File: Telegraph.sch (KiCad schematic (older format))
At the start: 16 parts

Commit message: Bump to v2 and add board layout
This design is intended for using a Raspberry Pi W and adds a header to
connect the Raspberry pi directly to the board. This also adds a PCB
speaker along with a transistor to amplify it, and a switching power
supply (prefab module). The transistor for the magnets is replaced by a
MOSFET (which has better specs and mostly a cuter package than the
TIP12x that was on there).
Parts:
- removed SHIELD?: ARDUINO_UNO, symbol ARDUINO_UNO
- removed U?: POLOLU_DRV8825, symbol POLOLU_DRV8825
- added A1: Pololu_Breakout_DRV8825, Modules:Pololu_Breakout-16_15.2x20.3mm, symbol Pololu_Breakout_DRV8825
- added C2, C3: 10uF, Capacitors_THT:CP_Radial_D5.0mm_P2.00mm, symbol CP
- added J1: Raspberry_Pi_2_3, Footprints:Raspberry_Pi_Zero, symbol Raspberry_Pi_2_3
- added P1: SPK, Pin_Headers:Pin_Header_Angled_1x02_Pitch2.54mm, symbol CONN_01X02
- added P5: FTDI-DEVICE, Pin_Headers:Pin_Header_Angled_1x06_Pitch2.54mm, symbol FTDI-DEVICE
- added Q1: STU60N3LH5, TO_SOT_Packages_THT:TO-251AA, symbol STU60N3LH5
- added R1: 1K, Resistors_THT:R_Axial_DIN0207_L6.3mm_D2.5mm_P10.16mm_Horizontal, symbol R
- added R2: 47R, Resistors_THT:R_Axial_DIN0207_L6.3mm_D2.5mm_P10.16mm_Horizontal, symbol R
- added REG1: REGULATOR_MODULE, Footprints:HCJ-IPM-V2, symbol REGULATOR_MODULE
- added RV1: 1K, Potentiometers:Potentiometer_Trimmer_ACP_CA9v_Horizontal_Px10.0mm_Py5.0mm, symbol POT
- added SW1: SW_Push, Buttons_Switches_THT:SW_Tactile_SPST_Angled_PTS645Vx58-2LFS, symbol SW_Push
- C1: renamed from C?; footprint (none) -> Capacitors_THT:CP_Radial_D8.0mm_P3.50mm
- CON1: renamed from CON?; footprint (none) -> Connectors:BARREL_JACK
- D1: renamed from D?; footprint (none) -> Diodes_THT:D_DO-41_SOD81_P10.16mm_Horizontal
- JP1: renamed from JP?; value Jumper_NO_Small -> A4988; footprint (none) -> Pin_Headers:Pin_Header_Straight_1x02_Pitch2.54mm
- JP2: renamed from JP?; value Jumper_NO_Small -> M0; footprint (none) -> Pin_Headers:Pin_Header_Straight_1x02_Pitch2.54mm
- JP3: renamed from JP?; value Jumper_NO_Small -> M1; footprint (none) -> Pin_Headers:Pin_Header_Straight_1x02_Pitch2.54mm
- JP4: renamed from JP?; value Jumper_NO_Small -> M2; footprint (none) -> Pin_Headers:Pin_Header_Straight_1x02_Pitch2.54mm
- P2, P4: renamed from P?; footprint (none) -> Pin_Headers:Pin_Header_Angled_1x02_Pitch2.54mm
- P3: renamed from P?; footprint (none) -> Pin_Headers:Pin_Header_Angled_1x04_Pitch2.54mm
- Q2: renamed from Q?; value TIP120 -> STU60N3LH5; footprint TO-220 -> TO_SOT_Packages_THT:TO-251AA; symbol TIP120 -> STU60N3LH5
- R3, R4: renamed from R?; footprint (none) -> Resistors_Universal:Resistor_SMD+THTuniversal_0805to1206_RM10_HandSoldering
- SP1: renamed from SP?; footprint (none) -> Buzzers_Beepers:Buzzer_15x7.5RM7.6
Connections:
- net +12V: now also A1.8 (VMOT), C2.1, REG1.2 (IN+)
- net +5V: now also JP2.1, JP3.1, JP4.1, A1.13 (~RST), A1.14 (~SLP), C3.1, J1.2 (5V), J1.4 (5V), R2.1, REG1.4 (OUT+); no longer JP2.2, JP3.2, JP4.2
- net DIR: now also A1.16 (DIR), J1.31 (GPIO6)
- net EN: now also A1.9 (~EN), J1.37 (GPIO26)
- net GND: now also A1.1 (GND), A1.7 (GND), C2.2, C3.2, J1.14 (GND), J1.20 (GND), J1.25 (GND), J1.30 (GND), J1.34 (GND), J1.39 (GND), J1.6 (GND), J1.9 (GND), P5.1 (GND), Q1.3 (S), REG1.1 (IN-), REG1.3 (OUT-), SW1.1; no longer SP1.2
- net KEY: now also J1.11 (GPIO17_(GEN0))
- net MAGNET: now also J1.36 (GPIO16)
- net SPK: now also J1.12 (GPIO18_(GEN1)), R1.2; no longer SP1.1
- net STEP: now also A1.15 (STEP), J1.33 (GPIO13)
- net at JP1.2: now also A1.2 (~FLT)
- net at P3.1 (P1): now also A1.6 (B2)
- net at P3.2 (P2): now also A1.5 (B1)
- net at P3.3 (P3): now also A1.4 (A1)
- net at P3.4 (P4): now also A1.3 (A2)
- new net: A1.11 (M1), JP3.2
- new net: A1.12 (M2), JP4.2
- new net: A1.10 (M0), JP2.2
- new net: P1.2 (P2), RV1.1, SP1.1
- new net: P1.1 (P1), Q1.2 (D), SP1.2
- new net: Q1.1 (G), R1.1
- new net: R2.2, RV1.2
- new net PWR: J1.5 ((SCL1)_GPIO3), SW1.2
- new net RX: J1.10 ((RXD0)_GPIO15), P5.4 (RX)
- new net TX: J1.8 ((TXD0)_GPIO14), P5.5 (TX)
- no-connect marks 1 -> 26
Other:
- moved on the sheet: C1, CON1, D1, P2, P3, P4, R3, R4, SP1

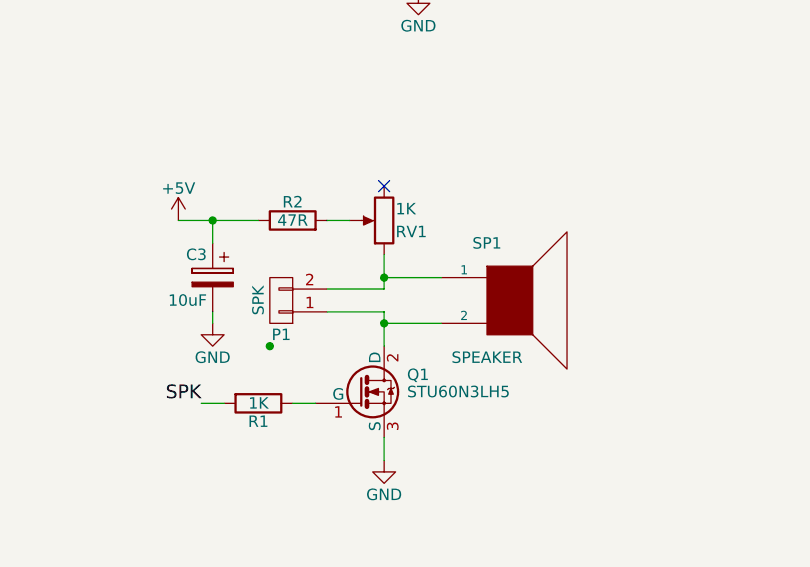
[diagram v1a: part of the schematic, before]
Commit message: Improve values for speaker
The previous resistor values were more conservative, based on another
speaker.  Testing with the actual speaker, whose type number was also
addd to the schematic, suggests smaller resistor values will work
better.
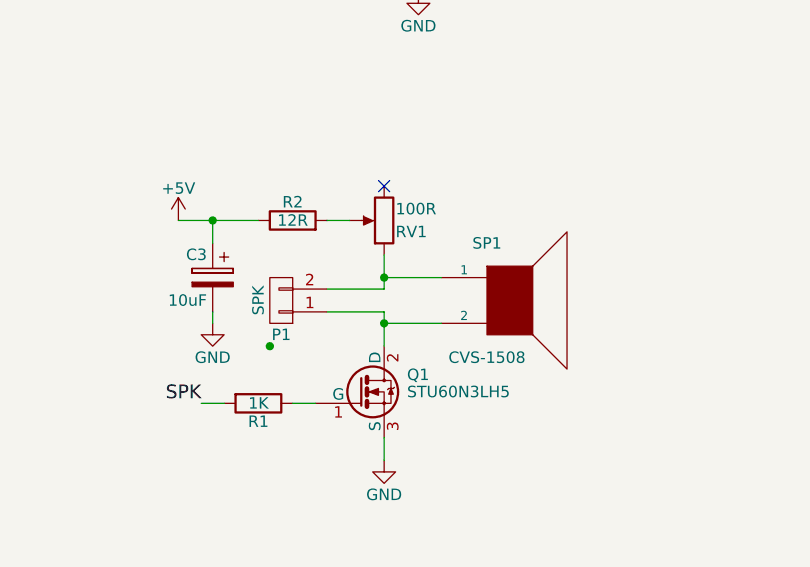
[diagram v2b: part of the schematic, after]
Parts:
- R2: value 47R -> 12R
- RV1: value 1K -> 100R
- SP1: value SPEAKER -> CVS-1508
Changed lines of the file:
@@
 P 7550 4100
 F 0 "SP1" H 7450 4350 50  0000 C CNN
-F 1 "SPEAKER" H 7450 3850 50  0000 C CNN
+F 1 "CVS-1508" H 7450 3850 50  0000 C CNN
 F 2 "Buzzers_Beepers:Buzzer_15x7.5RM7.6" H 7550 4100 50  0001 C CNN
 F 3 "" H 7550 4100 50  0000 C CNN
@@
 P 6600 3750
 F 0 "R2" V 6680 3750 50  0000 C CNN
-F 1 "47R" V 6600 3750 50  0000 C CNN
+F 1 "12R" V 6600 3750 50  0000 C CNN
 F 2 "Resistors_THT:R_Axial_DIN0207_L6.3mm_D2.5mm_P10.16mm_Horizontal" V 6530 3750 50  0001 C CNN
 F 3 "" H 6600 3750 50  0000 C CNN
@@
 P 7000 3750
 F 0 "RV1" H 6950 3800 50  0000 R CNN
-F 1 "1K" H 6950 3700 50  0000 R CNN
+F 1 "100R" H 6950 3700 50  0000 R CNN
 F 2 "Potentiometers:Potentiometer_Trimmer_ACP_CA9v_Horizontal_Px10.0mm_Py5.0mm" H 7000 3750 50  0001 C CNN
 F 3 "" H 7000 3750 50  0001 C CNN

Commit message: Convert to KiCad 5
There might be other changes too, I did not commit this right away...
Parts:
- A1: symbol Pololu_Breakout_DRV8825 -> Driver_Motor:Pololu_Breakout_DRV8825
- C1, C2, C3: symbol CP -> Device:CP
- CON1: symbol BARREL_JACK -> Connector_Specialized:Barrel_Jack
- D1: symbol D -> Device:D
- J1: symbol Raspberry_Pi_2_3 -> Connector_Specialized:Raspberry_Pi_2_3
- JP1: symbol Jumper_NO_Small -> Device:Jumper_NO_Small
- JP2, JP3, JP4: symbol Jumper_NC_Small -> Device:Jumper_NC_Small
- P1, P2, P4: symbol CONN_01X02 -> Connector_Generic:Conn_01x02
- P3: symbol CONN_01X04 -> Connector_Generic:Conn_01x04
- P5: symbol FTDI-DEVICE -> Components:FTDI-DEVICE
- Q1, Q2: symbol STU60N3LH5 -> Components:STU60N3LH5
- R1, R2, R3, R4: symbol R -> Device:R
- REG1: symbol REGULATOR_MODULE -> Components:REGULATOR_MODULE
- RV1: symbol POT -> Device:POT
- SP1: symbol SPEAKER -> Device:Speaker
- SW1: symbol SW_Push -> Switch:SW_Push
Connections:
- wire segments 96 -> 116
